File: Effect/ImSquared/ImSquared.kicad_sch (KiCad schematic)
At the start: 37 parts, among them J1 Conn_01x04_Pin, J2 Conn_01x03_Pin, Q1 DMMT5551, Q2 DMMT5551, Q3 DMMT5551, Q4 DMMT5551, U1 OPA1656, U2 OPA1656

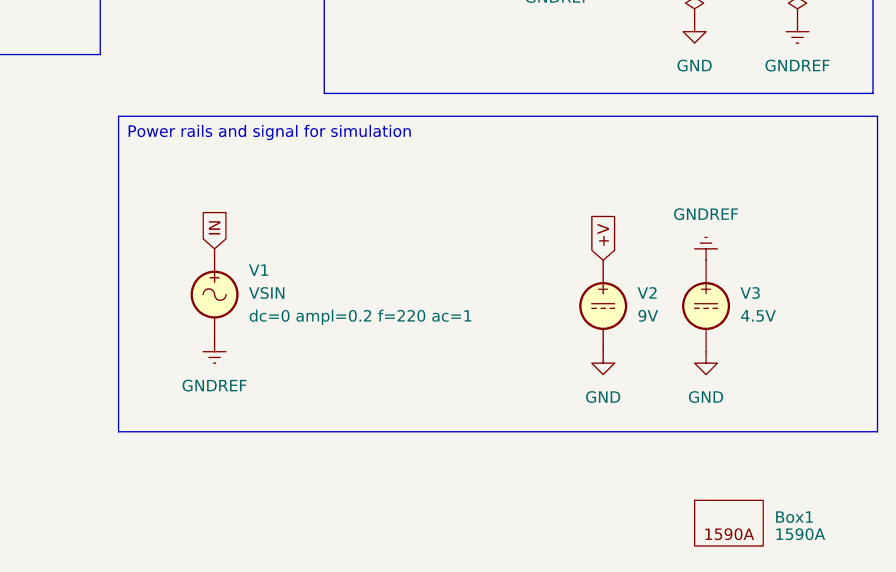
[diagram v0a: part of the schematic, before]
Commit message: Use better signals for simulation
I really need to learn not to use a sine signal for simulation input
testing: it makes the output look artificially good and hides problems.

I had fixed that problem for the control voltage in the multiplier
circuit, but then never did it for the main input signal, because the
end result looked so "obviously correct".

But then I got suspicious, and sure enough, when I start using a more
interesting main signal the picture changes.  It's not doing a proper
multiplication in the ImSquared circuit.  Maybe that might be ok for
sound, but it's not what I wanted the circuit to actually do.

Yes, VSIN is really easy to use, and it's a pain to set up something
even as simple as a triangle wave, and ngspice seems to get unhappier
about abrupt edges so simulation is more prone to problems.

But making a signal that is more triangle-wave like is not _that_ hard,
and at least shows when the end result has soft clipping or other simple
issues, and sure enough...

Note that the multiplier itself seems ok.  The problem is in the
ImSquared circuit, and I think I see what it is: blending in the
original signal - even when it's not used - messes up the impedance of
the input signal to the multiplier, and I may just need to add a buffer
there too.

This doesn't do that fix, this just fixes the simulation input so that
you can see the problem clearly.  Maybe some day I'll learn this lesson.

Signed-off-by: Linus Torvalds <torvalds@linux-foundation.org>
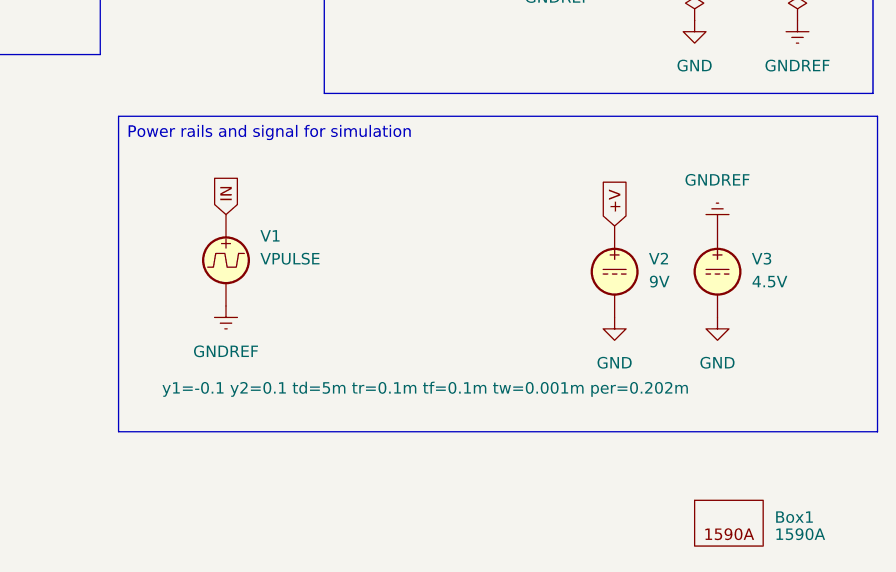
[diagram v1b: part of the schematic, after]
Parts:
- removed V1: VSIN, symbol Simulation_SPICE:VSIN
- added V1: VPULSE, symbol Simulation_SPICE:VPULSE
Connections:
- net GNDREF: now also V1.2
- net IN: now also V1.1
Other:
- moved on the sheet: V2, V3

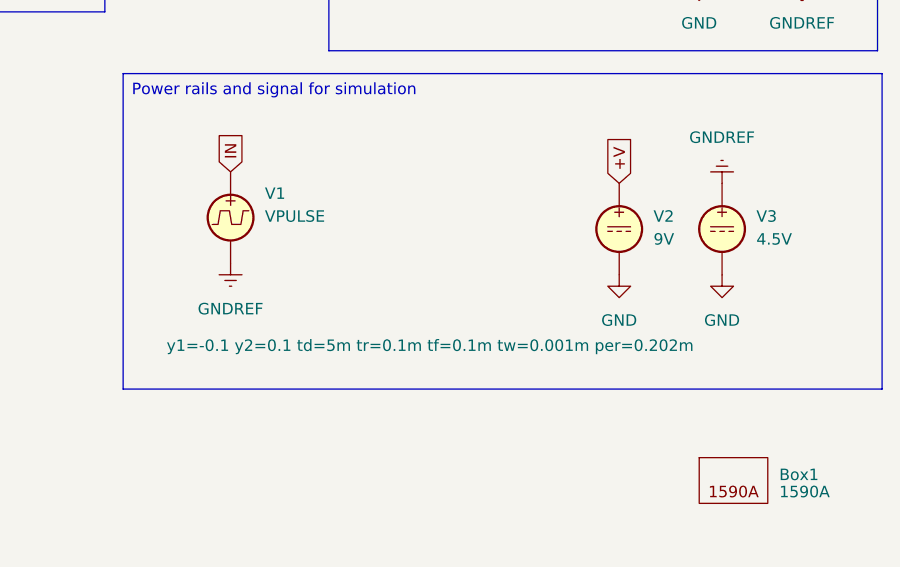
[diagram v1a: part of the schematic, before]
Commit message: Work on signal generation for simulation some more
It turns out that I was wrong about there being something wrong with the
ImSquared circuit: it seems to work just fine, and the fact that the
input signal gets used for both the blending and the multiplier input
appears perfectly ok.

The impedance into the multiplier should be very high as-is.  Famous
last confused words.

What confused me was misreading the output signal: I had expected hard
edges from the triangle input, and so I assumed that the soft curve was
due to some saturation or soft clipping issue and was blaming something
going wrong in the circuit.

But that was a complete thinko: the soft output curve was in fact just
the parabola of the triange wave (locally a linear "y=ax+b" function
when *not* looking at the peaks) being squared and becoming second-order
function ("y=az^2+b").

So those soft signals had nothing to do with the actual peaks of the
triangle - quite the opposite.  They were from the linear part of the
triangle wave when it switched signs.

Ergo, it actually worked exactly as designed, and I just misread the
output because I didn't line up the peaks and troughs correctly.

That said, the input signal is still much too simplistic.  The triangle
wave was better than a pure sine wave, but I want more dynamic range to
see any actual clipping issues.  So of the native signal generator
functions, let's try the amplitude-modulated signal instead, which gives
a combination of "quiet" and "loud" sections.

That already shows an interesting artifact: the output signal is
obviously a linear function of the current (it's the voltage drop over
the resistor R2), and I was naively expecting it to be centered around a
center voltage (the "half of the 1mA current" point, so roughly centered
at 8V in between the 7-9V peaks).

And it *is* technically centered right around the expected location, but
it's the *differential* output Vd(OUT1,OUT2) that is so centered.

And we obviously only tap one side (OUT1)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
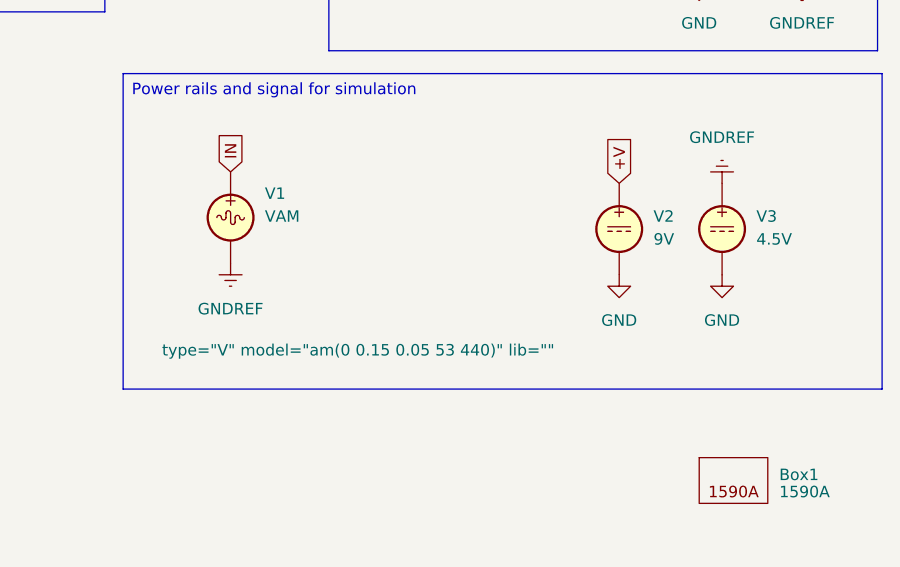
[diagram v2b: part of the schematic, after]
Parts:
- removed V1: VPULSE, symbol Simulation_SPICE:VPULSE
- added V1: VAM, symbol Simulation_SPICE:VAM
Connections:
- net GNDREF: now also V1.2
- net IN: now also V1.1
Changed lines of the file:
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@@
 	)
 	(symbol
-		(lib_id "Simulation_SPICE:VPULSE")
-		(at 209.55 144.78 0)
-		(unit 1)
-		(exclude_from_sim no)
-		(in_bom yes)
-		(on_board yes)
-		(dnp no)
-		(property "Reference" "V1"
-			(at 213.36 142.1101 0)
-			(effects
-				(font
-					(size 1.27 1.27)
-				)
-				(justify left)
-			)
-		)
-		(property "Value" "VPULSE"
-			(at 213.36 144.6501 0)
-			(effects
-				(font
-					(size 1.27 1.27)
-				)
-				(justify left)
-			)
-		)
-		(property "Footprint" ""
-			(at 209.55 144.78 0)
-			(effects
-				(font
-					(size 1.27 1.27)
-				)
-				(hide yes)
-			)
-		)
-		(property "Datasheet" "https://ngspice.sourceforge.io/docs/ngspice-html-manual/manual.xhtml#sec_Independent_Sources_for"
-			(at 209.55 144.78 0)
-			(effects
-				(font
-					(size 1.27 1.27)
-				)
-				(hide yes)
-			)
-		)
-		(property "Description" "Voltage source, pulse"
-			(at 209.55 144.78 0)
-			(effects
-				(font
-					(size 1.27 1.27)
-				)
-				(hide yes)
-			)
-		)
-		(property "Sim.Pins" "1=+ 2=-"
-			(at 209.55 144.78 0)
-			(effects
-				(font
-					(size 1.27 1.27)
-				)
-				(hide yes)
-			)
-		)
-		(property "Sim.Type" "PULSE"
-			(at 209.55 144.78 0)
-			(effects
-				(font
-					(size 1.27 1.27)
-				)
-				(hide yes)
-			)
-		)
-		(property "Sim.Device" "V"
-			(at 209.55 144.78 0)
-			(effects
-				(font
-					(size 1.27 1.27)
-				)
-				(justify left)
-				(hide yes)
-			)
-		)
-		(property "Sim.Params" "y1=-0.1 y2=0.1 td=5m tr=0.1m tf=0.1m tw=0.001m per=0.202m"
-			(at 202.438 159.004 0)
-			(effects
-				(font
-					(size 1.27 1.27)
-				)
-				(justify left)
-			)
-		)
-		(pin "2"
-		)
-		(pin "1"
-		)
-		(instances
-			(project ""
-				(path "/9e337e0b-885b-4d2b-99a2-62cdd082c615"
-					(reference "V1")
-					(unit 1)
-				)
-			)
-		)
-	)
-	(symbol
 		(lib_id "Connector:Conn_01x04_Pin")
 		(at 229.87 95.25 0)
@@
 					(unit 1)
 				)
+			)
+		)
+	)
+	(symbol
+		(lib_id "Simulation_SPICE:VAM")
+		(at 209.55 144.78 0)
+		(unit 1)
+		(exclude_from_sim no)
+		(in_bom yes)
+		(on_board yes)
+		(dnp no)
+		(property "Reference" "V1"
+			(at 213.36 142.1101 0)
+			(effects
+				(font
+					(size 1.27 1.27)
+				)
+				(justify left)
+			)
+		)
+		(property "Value" "VAM"
+			(at 213.36 144.6501 0)
+			(effects
+				(font
+					(size 1.27 1.27)
+				)
+				(justify left)
+			)
+		)
+		(property "Footprint" ""
+			(at 209.55 144.78 0)
+			(effects
+				(font
+					(size 1.27 1.27)
+				)
+				(hide yes)
+			)
+		)
+		(property "Datasheet" "https://ngspice.sourceforge.io/docs/ngspice-html-manual/manual.xhtml#sec_Independent_Sources_for"
+			(at 209.55 144.78 0)
+			(effects
+				(font
+					(size 1.27 1.27)
+				)
+				(hide yes)
+			)
+		)
+		(property "Description" "Voltage source, AM"
+			(at 209.55 144.78 0)
+			(effects
+				(font
+					(size 1.27 1.27)
+				)
+				(hide yes)
+			)
+		)
+		(property "Sim.Pins" "1=1 2=2"
+			(at 209.55 144.78 0)
+			(effects
+				(font
+					(size 1.27 1.27)
+				)
+				(hide yes)
+			)
+		)
+		(property "Sim.Device" "SPICE"
+			(at 209.55 144.78 0)
+			(effects
+				(font
+					(size 1.27 1.27)
+				)
+				(justify left)
+				(hide yes)
+			)
+		)
+		(property "Sim.Params" "type=\"V\" model=\"am(0 0.15 0.05 53 440)\" lib=\"\""
+			(at 201.93 159.512 0)
+			(effects
+				(font
+					(size 1.27 1.27)
+				)
+				(justify left)
+			)
+		)
+		(pin "1"
+		)
+		(pin "2"
+		)
+		(instances
+			(project ""
+				(path "/9e337e0b-885b-4d2b-99a2-62cdd082c615"
+					(reference "V1")
+					(unit 1)
+				)

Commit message: ImSquared: fix enormously stupid mistake
Capacitors C1/C2 had been marked "Exclude from board", because they were
copied from a test capacitor I had in a sim-only circuit.  And I didn't
notice at any point that the PCB design didn't have them.

Not even when populating the board.  I did notice that the components on
the BOM started from C3, and I just idly thought - without looking any
closer at it - that I had forgotten to re-annotate the circuit.

So I never gave it another thought - until none of the signal actually
made it to the analog multiplier unit, so the board didn't actually work
at all.  D'oh!

Trivial fix, but oh how annoying.  KiCad makes it visually clear when a
component is excluded from simulation, and when a component is marked
"Do not populate".  But something marked "Exclude from board" is clearly
too easy to miss.  I need to be more careful.

I was able to bodge-wire this, with three of four endpoints of the two
mislaid caps being through-hole (the 'IN' signal source, and two
potentiometer pins).  For the fourth signal ('OUT1') I just soldered a
wire to the 2.2kOhm resistor.

I _hate_ soldering wire and my bodge wires weren't pretty.  But the
alternative was "wait a week for fixed boards to test because you're a
dum-dum".

The circuit does actually work and seems to behave exactly like in
simulation.  Lovely.

Signed-off-by: Linus Torvalds <torvalds@linux-foundation.org>
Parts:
- C1, C2: footprint (none) -> Mylib:C_0704_1810Metric; now in the parts list
- V1, V2, V3: now left out of the parts list
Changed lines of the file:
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@@
 		(unit 1)
 		(exclude_from_sim no)
-		(in_bom no)
-		(on_board no)
+		(in_bom yes)
+		(on_board yes)
 		(dnp no)
 		(fields_autoplaced yes)
@@
 			)
 		)
-		(property "Footprint" ""
+		(property "Footprint" "Mylib:C_0704_1810Metric"
 			(at 144.78 87.3252 0)
 			(effects
@@
 		(unit 1)
 		(exclude_from_sim no)
-		(in_bom yes)
+		(in_bom no)
 		(on_board no)
 		(dnp no)
@@
 		(unit 1)
 		(exclude_from_sim no)
-		(in_bom yes)
+		(in_bom no)
 		(on_board no)
 		(dnp no)
@@
 		(unit 1)
 		(exclude_from_sim no)
-		(in_bom no)
-		(on_board no)
+		(in_bom yes)
+		(on_board yes)
 		(dnp no)
 		(fields_autoplaced yes)
@@
 			)
 		)
-		(property "Footprint" ""
+		(property "Footprint" "Mylib:C_0704_1810Metric"
 			(at 143.51 35.2552 0)
 			(effects
@@
 		(unit 1)
 		(exclude_from_sim no)
-		(in_bom yes)
-		(on_board yes)
+		(in_bom no)
+		(on_board no)
 		(dnp no)
 		(property "Reference" "V1"

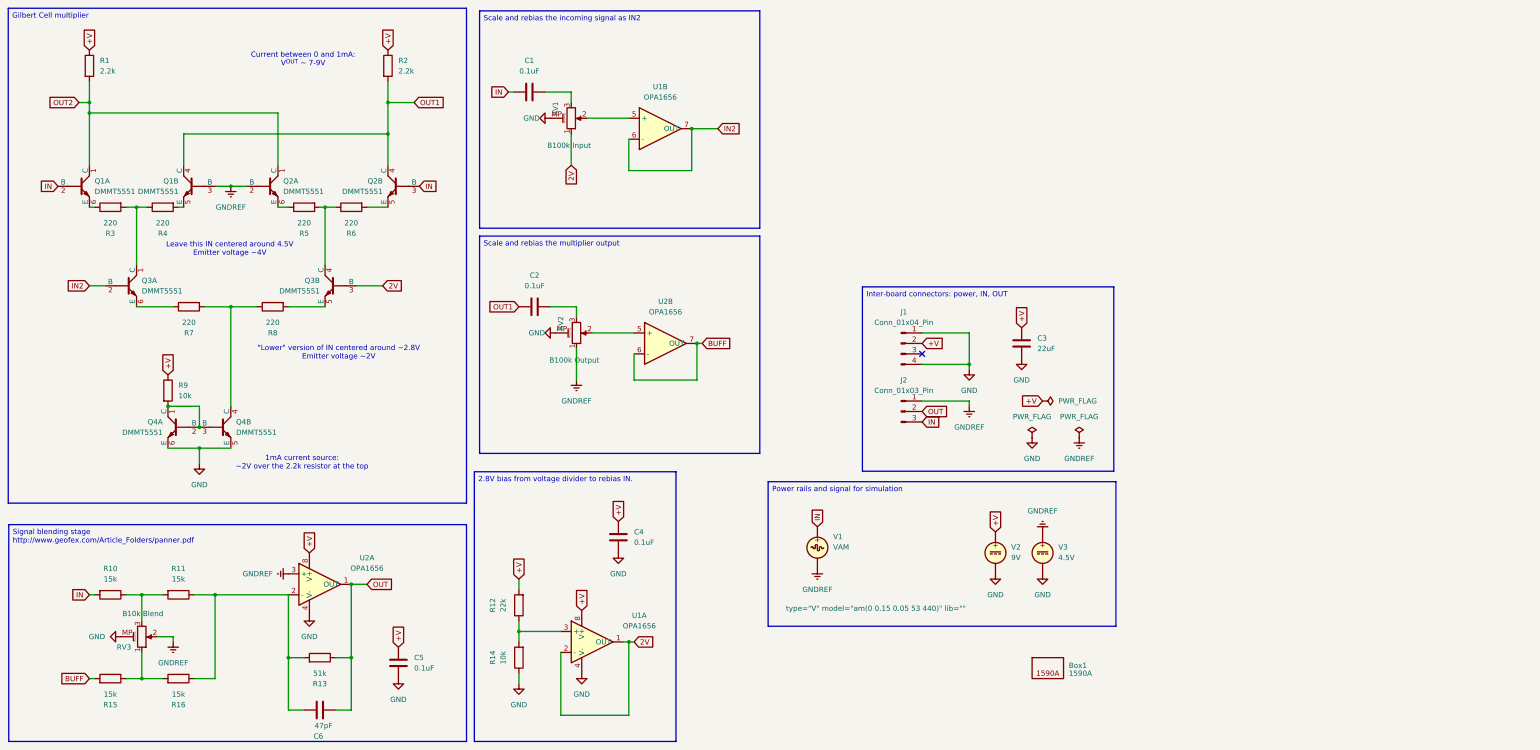
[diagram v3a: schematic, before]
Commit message: ImSquared: do the output using a differential amplifier setup
Honestly, this doesn't really change anything fundamental, it's just
another step in the endless saga of "Linus does completely useless
things just because he wants to learn about circuits".  And building a
differential amplifier out of three op-amps is certainly that.

Doing this also seemed to show that the OPA1656 actually has an
appreciable amount of current going into the inputs in simulation.  It
may be a real effect when the input is close to the positive power rail
(which is outside spec for the chip).  Or it's a simulation issue.  Or
it's me messing something else up.

Repeat after me: "It's not a failure, it's a learning experience".

I'm not happy about the blending circuit, it annoys me how it shows up
in several of the effects circuits and it doesn't add anything to the
experience.  It's needed for testing actual sound, though, but it makes
me wonder if I should just do it in all in the base board (especially
the active RJ45 version?)

I also need to bring real sound into simulation.  I guess I will need to
learn about using wav files as inputs to ngspice, instead of hacking up
random signal sources just to see the effect in simulation.

Too many things to learn.

Signed-off-by: Linus Torvalds <torvalds@linux-foundation.org>
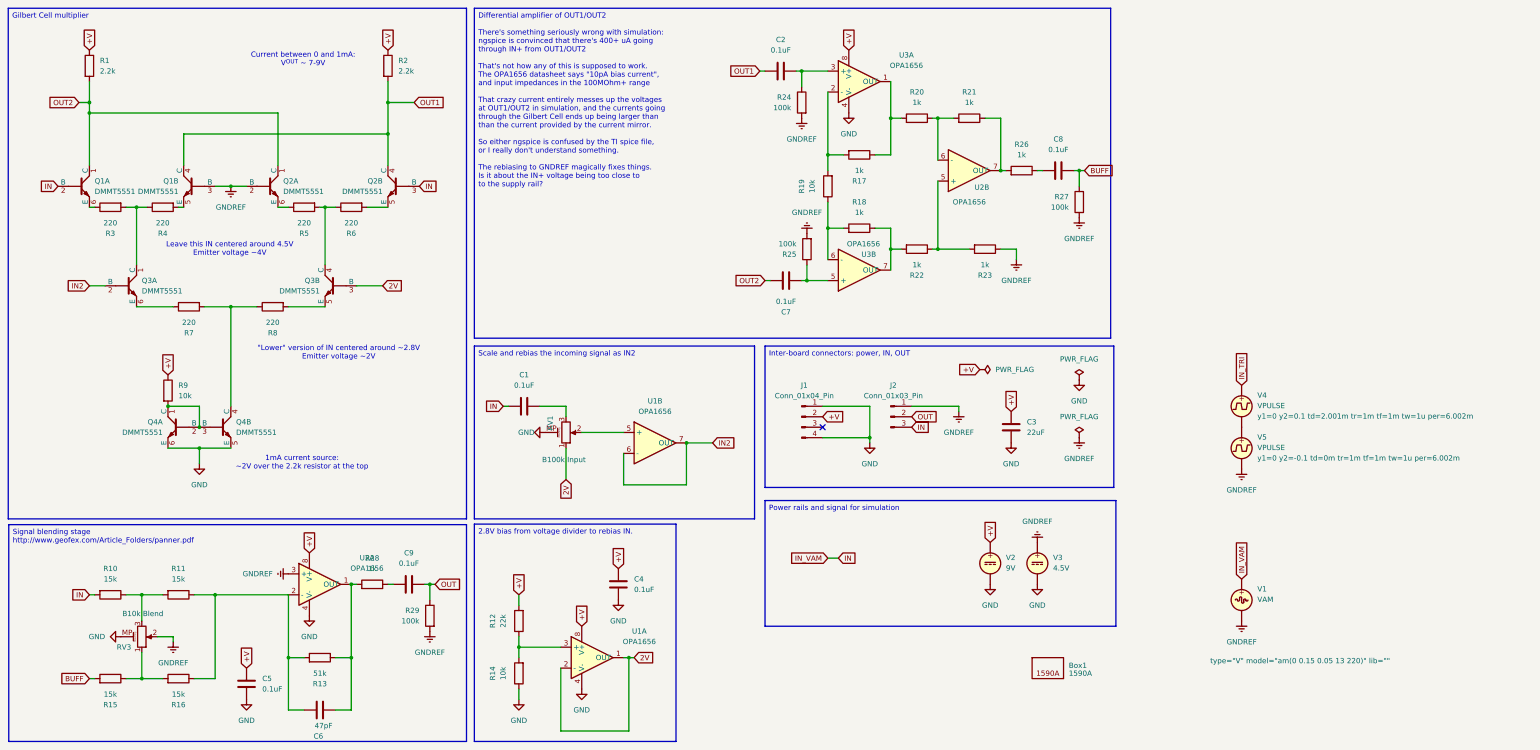
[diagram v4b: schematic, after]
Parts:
- removed RV2: B100k Output, Mylib:Potentiometer_9mm_MP, symbol Device:R_Potentiometer_MountingPin
- added C7, C8, C9: 0.1uF, Mylib:C_0704_1810Metric, symbol Device:C
- added R17, R18, R20, R21, R22, R23, R26, R28: 1k, Resistor_SMD:R_0805_2012Metric, symbol Device:R
- added R19: 10k, Resistor_SMD:R_0805_2012Metric, symbol Device:R
- added R24, R25, R27, R29: 100k, Resistor_SMD:R_0805_2012Metric, symbol Device:R
- added U3: OPA1656, Package_SO:SOIC-8_3.9x4.9mm_P1.27mm, symbol Mylib:OPA1656
- added V4, V5: VPULSE, symbol Simulation_SPICE:VPULSE
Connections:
- net +V: now also U3.8 (V+)
- net BUFF: now also C8.2, R27.1; no longer U2.6 (-), U2.7 (OUT)
- net GND: now also U3.4 (V-)
- net GNDREF: now also R23.1, R24.2, R25.2, R27.2, R29.2, V5.2
- net OUT: now also C9.2, R29.1; no longer C6.1, R13.1, U2.1 (OUT)
- net OUT2: now also C7.1
- net at U2.5 (+): now also R22.1, R23.2
- net at C2.2: now also R24.1, U3.3 (+)
- new net: R17.1, R20.2, U3.1 (OUT)
- new net: R17.2, R19.2, U3.2 (-)
- new net: R20.1, R21.2, U2.6 (-)
- new net: R21.1, R26.2, U2.7 (OUT)
- new net: C7.2, R25.1, U3.5 (+)
- new net: V4.2, V5.1
- new net: R18.2, R19.1, U3.6 (-)
- new net: C6.1, R13.1, R28.2, U2.1 (OUT)
- new net: R18.1, R22.2, U3.7 (OUT)
- new net: C8.1, R26.1
- new net: C9.1, R28.1
- new net IN_TRI: V4.1
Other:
- moved on the sheet: C1, C3, C4, C5, J1, J2, R12, R14, RV1, U1A, U1B, U2B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
